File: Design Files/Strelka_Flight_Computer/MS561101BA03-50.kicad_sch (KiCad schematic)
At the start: 2 parts

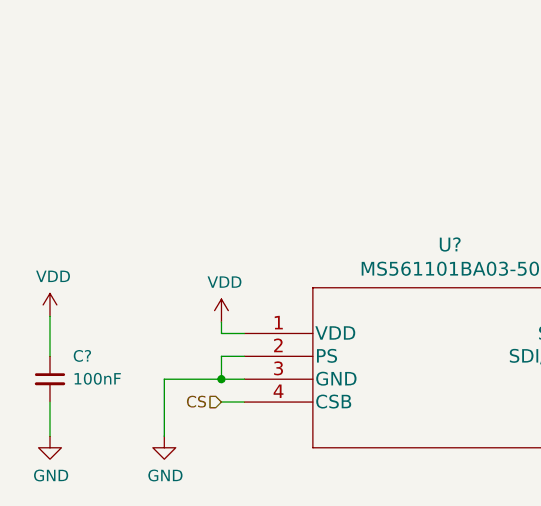
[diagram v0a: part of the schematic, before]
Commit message: Added new UBLOX GPS
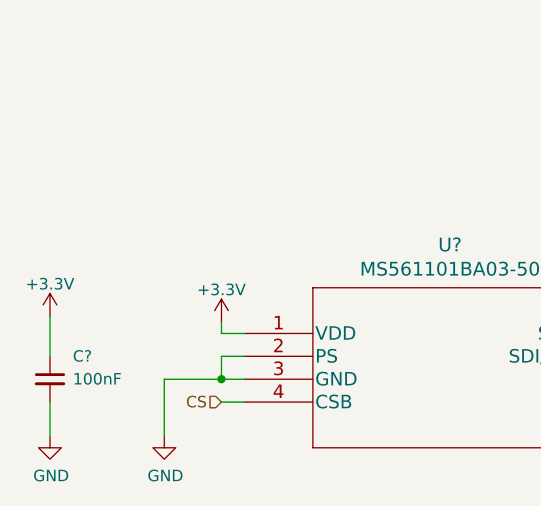
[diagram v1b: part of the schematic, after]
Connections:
- net VDD renamed +3V3
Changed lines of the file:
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@@
     (pin "2")
-  )
-  (symbol (lib_id "power:VDD") (at 123.825 88.265 0) (unit 1)
-    (in_bom yes) (on_board yes)
-    (property "Reference" "#PWR?" (id 0) (at 123.825 92.075 0)
-      (effects (font (size 1.27 1.27)) hide)
-    )
-    (property "Value" "VDD" (id 1) (at 124.206 83.8708 0))
-    (property "Footprint" "" (id 2) (at 123.825 88.265 0)
-      (effects (font (size 1.27 1.27)) hide)
-    )
-    (property "Datasheet" "" (id 3) (at 123.825 88.265 0)
-      (effects (font (size 1.27 1.27)) hide)
-    )
-    (pin "1")
-  )
-  (symbol (lib_id "power:VDD") (at 104.775 87.63 0) (unit 1)
-    (in_bom yes) (on_board yes)
-    (property "Reference" "#PWR?" (id 0) (at 104.775 91.44 0)
-      (effects (font (size 1.27 1.27)) hide)
-    )
-    (property "Value" "VDD" (id 1) (at 105.156 83.2358 0))
-    (property "Footprint" "" (id 2) (at 104.775 87.63 0)
-      (effects (font (size 1.27 1.27)) hide)
-    )
-    (property "Datasheet" "" (id 3) (at 104.775 87.63 0)
-      (effects (font (size 1.27 1.27)) hide)
-    )
-    (pin "1")
   )
   (symbol (lib_id "power:GND") (at 104.775 100.965 0) (unit 1)
@@
     )
     (property "Datasheet" "" (id 3) (at 104.775 100.965 0)
+      (effects (font (size 1.27 1.27)) hide)
+    )
+    (pin "1")
+  )
+  (symbol (lib_id "power:+3.3V") (at 104.775 87.63 0) (unit 1)
+    (in_bom yes) (on_board yes) (fields_autoplaced)
+    (property "Reference" "#PWR?" (id 0) (at 104.775 91.44 0)
+      (effects (font (size 1.27 1.27)) hide)
+    )
+    (property "Value" "+3.3V" (id 1) (at 104.775 84.0542 0))
+    (property "Footprint" "" (id 2) (at 104.775 87.63 0)
+      (effects (font (size 1.27 1.27)) hide)
+    )
+    (property "Datasheet" "" (id 3) (at 104.775 87.63 0)
       (effects (font (size 1.27 1.27)) hide)
     )
@@
     (pin "8")
   )
+  (symbol (lib_id "power:+3.3V") (at 123.825 88.265 0) (unit 1)
+    (in_bom yes) (on_board yes) (fields_autoplaced)
+    (property "Reference" "#PWR?" (id 0) (at 123.825 92.075 0)
+      (effects (font (size 1.27 1.27)) hide)
+    )
+    (property "Value" "+3.3V" (id 1) (at 123.825 84.6892 0))
+    (property "Footprint" "" (id 2) (at 123.825 88.265 0)
+      (effects (font (size 1.27 1.27)) hide)
+    )
+    (property "Datasheet" "" (id 3) (at 123.825 88.265 0)
+      (effects (font (size 1.27 1.27)) hide)
+    )
+    (pin "1")
+  )
 )

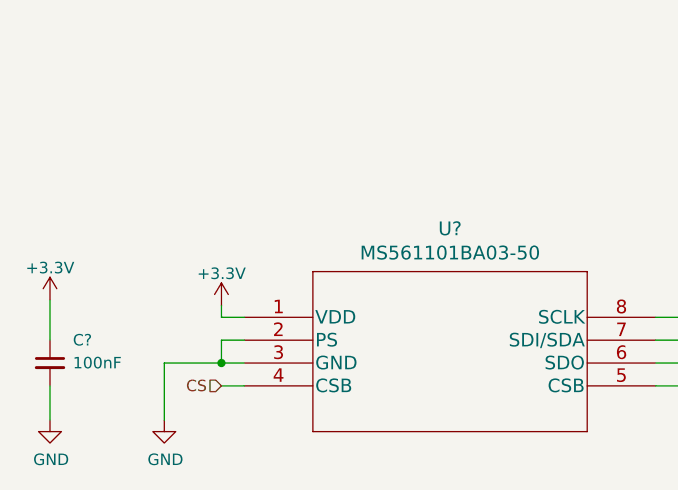
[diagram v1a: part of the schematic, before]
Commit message: Added motor driver to power board
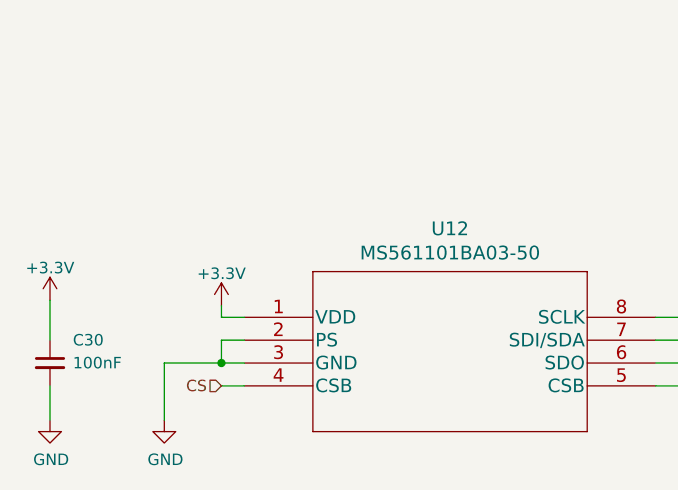
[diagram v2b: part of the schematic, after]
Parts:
- gave numbers to parts that had none: 2
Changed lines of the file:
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@@
   (symbol (lib_id "Device:C_Small") (at 104.775 94.615 0) (unit 1)
     (in_bom yes) (on_board yes)
-    (property "Reference" "C?" (id 0) (at 107.315 92.075 0)
+    (property "Reference" "C30" (id 0) (at 107.315 92.075 0)
       (effects (font (size 1.27 1.27)) (justify left))
     )
@@
   (symbol (lib_id "power:GND") (at 104.775 100.965 0) (unit 1)
     (in_bom yes) (on_board yes)
-    (property "Reference" "#PWR?" (id 0) (at 104.775 107.315 0)
+    (property "Reference" "#PWR0179" (id 0) (at 104.775 107.315 0)
       (effects (font (size 1.27 1.27)) hide)
     )
@@
   (symbol (lib_id "power:+3.3V") (at 104.775 87.63 0) (unit 1)
     (in_bom yes) (on_board yes) (fields_autoplaced)
-    (property "Reference" "#PWR?" (id 0) (at 104.775 91.44 0)
+    (property "Reference" "#PWR0178" (id 0) (at 104.775 91.44 0)
       (effects (font (size 1.27 1.27)) hide)
     )
@@
   (symbol (lib_id "power:GND") (at 117.475 100.965 0) (unit 1)
     (in_bom yes) (on_board yes)
-    (property "Reference" "#PWR?" (id 0) (at 117.475 107.315 0)
+    (property "Reference" "#PWR0180" (id 0) (at 117.475 107.315 0)
       (effects (font (size 1.27 1.27)) hide)
     )
@@
   (symbol (lib_id "MS561101BA03-50:MS561101BA03-50") (at 149.225 94.615 0) (unit 1)
     (in_bom yes) (on_board yes)
-    (property "Reference" "U?" (id 0) (at 149.225 79.7052 0)
+    (property "Reference" "U12" (id 0) (at 149.225 79.7052 0)
       (effects (font (size 1.524 1.524)))
     )
@@
   (symbol (lib_id "power:+3.3V") (at 123.825 88.265 0) (unit 1)
     (in_bom yes) (on_board yes) (fields_autoplaced)
-    (property "Reference" "#PWR?" (id 0) (at 123.825 92.075 0)
+    (property "Reference" "#PWR0181" (id 0) (at 123.825 92.075 0)
       (effects (font (size 1.27 1.27)) hide)
     )

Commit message: Started component placement
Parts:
- U12: footprint SON8_MS5611_TEC -> Footprints:MS561101BA03-50
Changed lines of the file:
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@@
       (effects (font (size 1.524 1.524)))
     )
-    (property "Footprint" "SON8_MS5611_TEC" (id 2) (at 149.225 83.439 0)
+    (property "Footprint" "Footprints:MS561101BA03-50" (id 2) (at 149.225 83.439 0)
       (effects (font (size 1.524 1.524)) hide)
     )
